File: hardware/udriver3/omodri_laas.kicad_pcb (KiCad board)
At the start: 6 copper layers, 50 x 50 mm, 219 parts, among them J1 Conn_01x11, J10 Conn_01x07, J11 Conn_01x03, J12 Conn_01x03, J13 Conn_01x02, J14 Conn_01x40, J2 Conn_01x05, J3 Conn_01x03, J4 Conn_01x03, J5 Conn_01x05, J6 Conn_01x05, J7 Conn_01x02, J8 Conn_01x07, J9 Conn_02x04_Odd_Even, Q1 CSD88599Q5DC, Q2 CSD88599Q5DC, Q3 CSD88599Q5DC, Q4 CSD88599Q5DC, Q5 CSD88599Q5DC, Q6 CSD88599Q5DC, Q7 NX7002BKM, SW1 B3U-3100P, U1 TMS320F28388D, U10 DSLVDS1048, U11 TPS3703, U12 TPS3703, U13 TPD6E05U06, U14 DSLVDS1047, U15 TPD2E001, U16 TPD3E001, U19 DRV8353S, U2 MAX17502FxTB, U20 DRV8353S, U3 MPM3804GG, U4 MPM3804GG, U5 LT6654AIS6-3, U6 TPD3E001, U7 TXB0106, U8 TCAN332G, U9 TPD6E05U06, X1 ECS-TXO-2016-33-200-TR

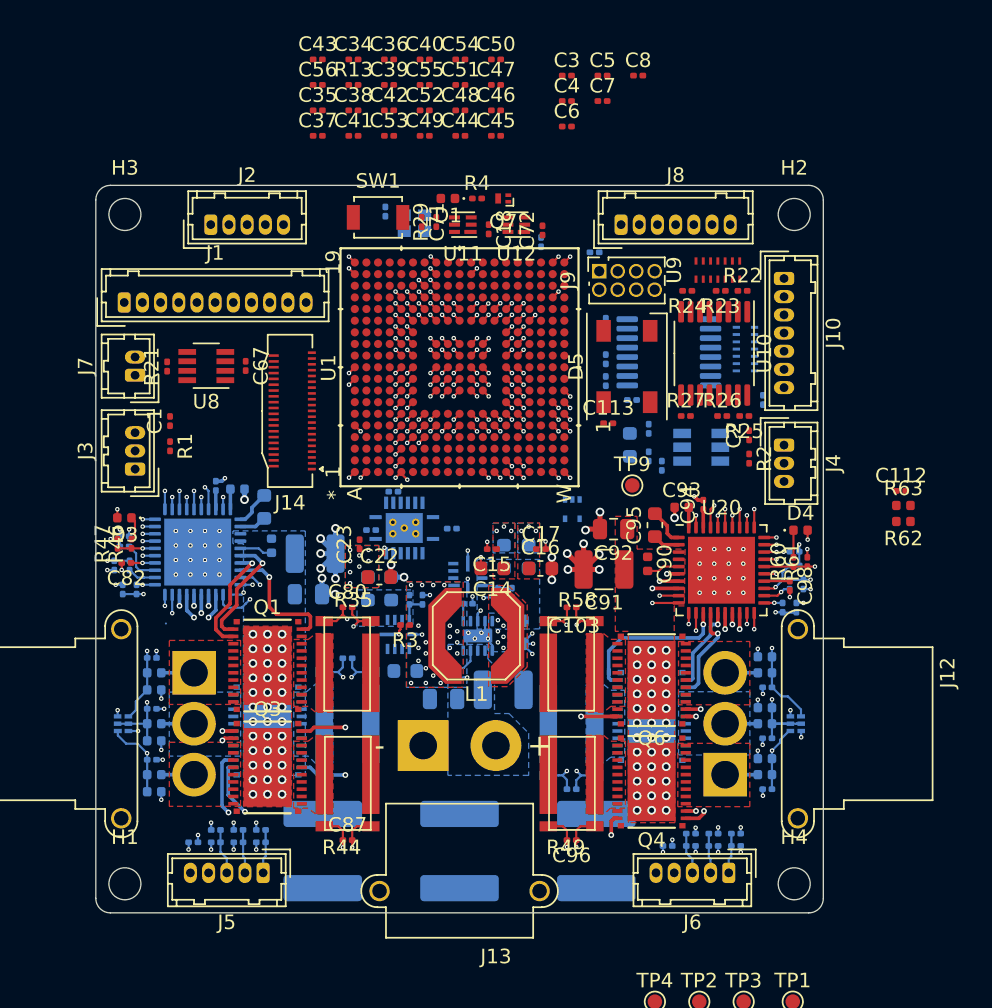
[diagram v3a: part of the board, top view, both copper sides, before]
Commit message: Routing update. All analog and DRV signals are wired. TMS mcu decoupling capacitors are in place.
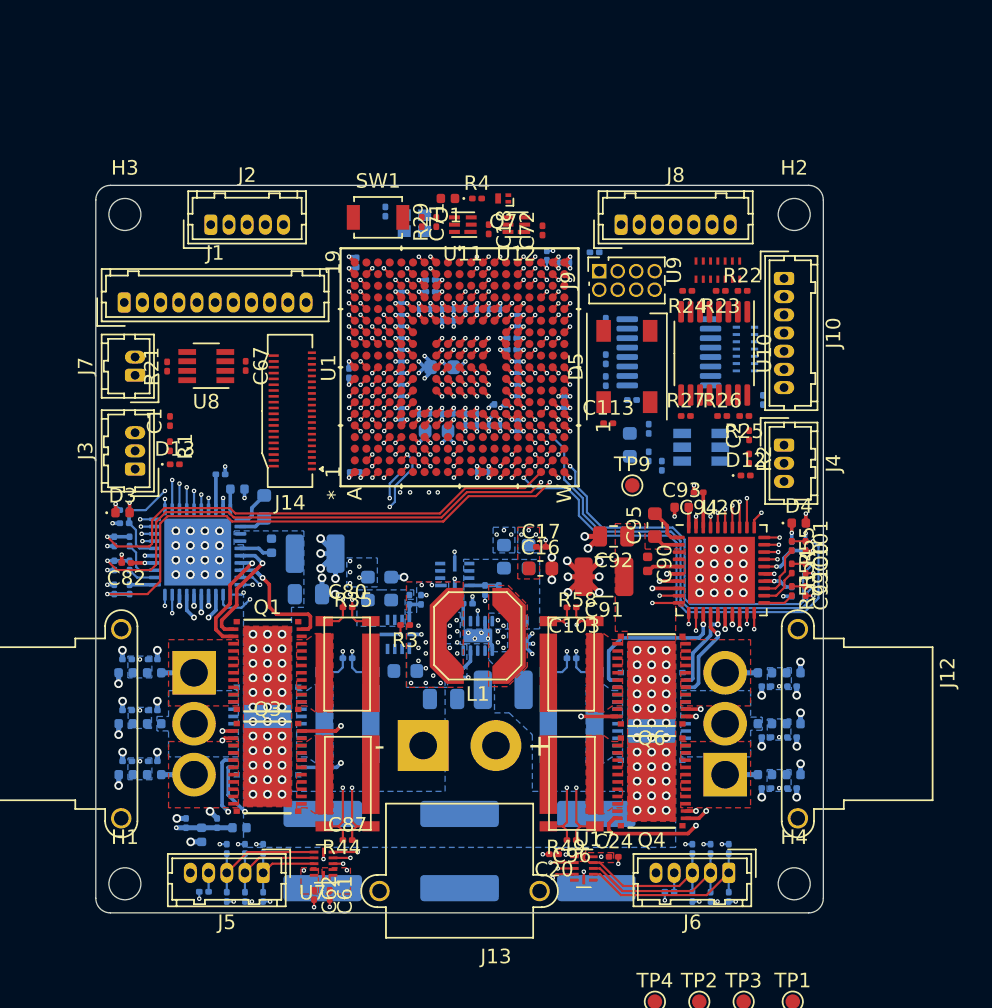
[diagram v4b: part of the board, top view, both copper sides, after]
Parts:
- removed R20: 1k, Resistor_SMD:R_0201_0603Metric
- removed U15: TPD2E001, Package_SO:Texas_R-PDSO-N5
- removed U16, U6: TPD3E001, udriver3:USON_6
- added C20: 100nF, Capacitor_SMD:C_0201_0603Metric, F.Cu at (131.5, 96.0)
- added C24: 100nF, Capacitor_SMD:C_0201_0603Metric, F.Cu at (135.6, 96.1)
- added D10: TPD1E04U04, Diode_SMD:D_0201_0603Metric, B.Cu at (102.2, 86.1)
- added D11: TPD1E04U04, Diode_SMD:D_0201_0603Metric, B.Cu at (106.2, 93.8)
- added D12: TPD1E04U04, Diode_SMD:D_0201_0603Metric, F.Cu at (144.7, 69.9)
- added D13: TPD1E04U04, Diode_SMD:D_0201_0603Metric, F.Cu at (105.4, 69.2)
- added D2: TPD1E04U04, Diode_SMD:D_0201_0603Metric, B.Cu at (147.8, 84.4)
- added D6: TPD1E04U04, Diode_SMD:D_0201_0603Metric, B.Cu at (147.8, 91.4)
- added D7: TPD1E04U04, Diode_SMD:D_0201_0603Metric, B.Cu at (147.8, 87.9)
- added D8: TPD1E04U04, Diode_SMD:D_0201_0603Metric, B.Cu at (102.2, 89.6)
- added D9: TPD1E04U04, Diode_SMD:D_0201_0603Metric, B.Cu at (102.2, 82.6)
- added U17: LSF0204RUT, Package_DFN_QFN:Texas_R_PUQFN-N12, F.Cu at (133.5, 96.9)
- C100, C101, C61, C62, C99, R51, R54, R55: moved to F.Cu
- C112, C14, C15, C22, C23, C3, C34, C35, C36, C37, C38, C39, C4, C40, C41, C42, C43, C44, C45, C46, C47, C48, C49, C5, C50, C51, C52, C53, C54, C55, C56, C6, C7, C8, C98, R13, R46, R47, R60, R61, R62, R63: moved to B.Cu
- U7: value TXB0106 -> LSF0204RUT; footprint udriver3:PVQFN_17 -> Package_DFN_QFN:Texas_R_PUQFN-N12; moved to F.Cu
- moved R63 53.3 mm to (107.3, 94.6), turned to 270 degrees
- moved C112 52.3 mm to (108.3, 93.8), turned to 90 degrees
- moved R62 50.3 mm to (109.9, 94.2)
- moved C54 28.4 mm to (126.6, 69.7)
- moved C61 28.1 mm to (116.1, 98.8), turned to 270 degrees
- moved C36 25.8 mm to (125.8, 66.5)
- moved C62 25.4 mm to (115.0, 98.8), turned to 270 degrees
- moved C43 25.0 mm to (121.0, 65.7), turned to 270 degrees
- moved R13 24.0 mm to (125.8, 65.7)
- moved C55 23.8 mm to (132.2, 64.9), turned to 270 degrees
- moved C50 23.8 mm to (117.4, 62.9), turned to 90 degrees
- moved U7 23.7 mm to (115.7, 96.6), turned to 180 degrees
- moved C3 23.3 mm to (128.2, 65.4), turned to 90 degrees
- moved C53 23.2 mm to (117.8, 69.7), turned to 180 degrees
- moved C4 22.6 mm to (129.0, 66.5), turned to 270 degrees
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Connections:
- R56 pad 1: GND -> Net-(Q5-Pad12)
- R56 pad 2: /OMODRI_driver_M2/SNB -> /OMODRI_driver_M2/SPB
- R56 pad 3: /OMODRI_driver_M2/SPB -> /OMODRI_driver_M2/SNB
- R56 pad 4: Net-(Q5-Pad12) -> GND
- U7 pad 1: /OMODRI_GPIO/ENC1_CHA -> VDD_3V3
- U7 pad 10: /OMODRI_QuadEncod/ENC2_A -> Net-(U7-Pad10)
- U7 pad 11: /OMODRI_QuadEncod/ENC2_B -> 5V0
- U7 pad 12: /OMODRI_QuadEncod/ENC2_I -> VDD_3V3
- U7 pad 2: VDD_3V3 -> Net-(U7-Pad2)
- U7 pad 3: /OMODRI_GPIO/ENC1_CHB -> /OMODRI_GPIO/ENC1_CHA
- U7 pad 4: /OMODRI_GPIO/ENC1_CHI -> /OMODRI_GPIO/ENC1_CHB
- U7 pad 5: /OMODRI_GPIO/ENC2_CHI -> /OMODRI_GPIO/ENC1_CHI
- U7 pad 6: /OMODRI_GPIO/ENC2_CHB -> GND
- U7 pad 7: /OMODRI_GPIO/ENC2_CHA -> /OMODRI_QuadEncod/ENC1_I
- U7 pad 8: Net-(R20-Pad2) -> /OMODRI_QuadEncod/ENC1_B
- U7 pad 9: GND -> /OMODRI_QuadEncod/ENC1_A
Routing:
- net /OMODRI_GPIO/M1_Vbus: track 0.00 -> 55.0 mm, vias 0 -> 2
- net /OMODRI_GPIO/M1_Vc: track 5.48 -> 49.5 mm, vias 1 -> 2
- net GND: track 97.4 -> 139.3 mm, vias 181 -> 209
- net /OMODRI_GPIO/M1_Ic: track 1.43 -> 42.7 mm, vias 1 -> 3
- net /OMODRI_GPIO/M1_Vb: track 4.66 -> 45.4 mm, vias 1 -> 2
- net /OMODRI_GPIO/ENC2_CHA: track 0.00 -> 36.8 mm, vias 0 -> 2
- net /OMODRI_GPIO/ENC1_CHI: track 0.00 -> 36.4 mm, vias 0 -> 2
- net /OMODRI_GPIO/M1_Ib: track 1.52 -> 37.9 mm, vias 1 -> 3
- net /OMODRI_GPIO/ENC1_CHB: track 0.00 -> 36.1 mm, vias 0 -> 2
- net /OMODRI_GPIO/M1_Va: track 5.07 -> 40.9 mm, vias 1 -> 3
- net /OMODRI_GPIO/ENC1_CHA: track 0.00 -> 35.1 mm, vias 0 -> 2
- net /OMODRI_GPIO/ENC2_CHB: track 0.00 -> 34.3 mm, vias 0 -> 2
- net /OMODRI_GPIO/M1_Ia: track 1.18 -> 35.0 mm
- net /OMODRI_GPIO/ENC2_CHI: track 0.00 -> 33.4 mm, vias 0 -> 2
- net /OMODRI_driver_M2/INHA: track 0.84 -> 33.2 mm, vias 1 -> 3
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- added copper zone on B.Cu, net /OMODRI_GPIO/M1_Va
- added copper zone on B.Cu, net /OMODRI_GPIO/M1_Vb
- added copper zone on B.Cu, net /OMODRI_GPIO/M1_Vc
- added copper zone on B.Cu, net /OMODRI_GPIO/M2_Va
- added copper zone on B.Cu, net /OMODRI_GPIO/M2_Vb
- added copper zone on B.Cu, net /OMODRI_GPIO/M2_Vc
- added copper zone on GND.Cu, net GND
- removed copper zone on F.Cu, net VDD_1V2
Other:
- copper layers 6 -> 8

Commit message: First release of the fully routed OMODRI PCB from LAAS. (8 layers)
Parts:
- removed C113: 100nF, Capacitor_SMD:C_0201_0603Metric
- removed J14: Conn_01x40, Connector_FFC-FPC:JAE_FF0841SA1_2Rows-41Pins_P0.40mm_Horizontal
- removed TP1, TP2, TP3, TP4, TP9: TestPoint, TestPoint:TestPoint_Pad_D1.0mm
- added J15: ADM6_ADF6, udriver3:ADF6-10-XX.X-XXX-4-X-A-XR, B.Cu at (113.0, 65.0)
- added J16: ADM6_ADF6, udriver3:ADF6-10-XX.X-XXX-4-X-A-XR, B.Cu at (137.0, 65.0)
- added R7: 33, Resistor_SMD:R_0201_0603Metric, F.Cu at (126.8, 53.6)
- C1, C16, C17, C18, C72, D12, R1, R25, R26, R27, U11, U12: moved to B.Cu
- C69, R30: moved to F.Cu
- J1: footprint Connector_Hirose:Hirose_DF13-11P-1.25DSA_1x11_P1.25mm_Vertical -> udriver3:Hirose_DF13-11P-1.25DSA_1x11_P1.25mm_Vertical
- J10, J8: footprint Connector_Hirose:Hirose_DF13-07P-1.25DSA_1x07_P1.25mm_Vertical -> udriver3:Hirose_DF13-07P-1.25DSA_1x07_P1.25mm_Vertical
- J2, J5, J6: footprint Connector_Hirose:Hirose_DF13-05P-1.25DSA_1x05_P1.25mm_Vertical -> udriver3:Hirose_DF13-05P-1.25DSA_1x05_P1.25mm_Vertical
- J3, J4: footprint Connector_Hirose:Hirose_DF13-03P-1.25DSA_1x03_P1.25mm_Vertical -> udriver3:Hirose_DF13-03P-1.25DSA_1x03_P1.25mm_Vertical
- J7: footprint Connector_Hirose:Hirose_DF13-02P-1.25DSA_1x02_P1.25mm_Vertical -> udriver3:Hirose_DF13-02P-1.25DSA_1x02_P1.25mm_Vertical
- U2: footprint Package_DFN_QFN:TDFN-10-1EP_2x3mm_P0.5mm_EP0.9x2mm -> udriver3:TDFN-10-1EP_2x3mm_P0.5mm_EP0.9x2mm_ThermalVias
- X1: value ECS-TXO-2016-33-200-TR -> ECS-TXO-2016-33-250-TR; footprint Crystal:Crystal_SMD_2016-4Pin_2.0x1.6mm -> udriver3:Crystal_SMD_2016-4Pin_2.0x1.6mm; moved to F.Cu
- moved D12 38.8 mm to (105.9, 68.2), turned to 90 degrees
- moved D13 38.0 mm to (143.4, 69.5), turned to 90 degrees
- moved D5 28.7 mm to (108.2, 67.1), turned to 270 degrees
- moved C16 11.9 mm to (131.0, 64.4), turned to 90 degrees
- moved C18 10.3 mm to (119.0, 59.5), turned to 180 degrees
- moved C17 9.98 mm to (129.8, 64.9), turned to 90 degrees
- moved C73 9.04 mm to (133.8, 56.2), turned to 90 degrees
- moved U11 7.84 mm to (119.2, 57.6), turned to 90 degrees
- moved R30 7.65 mm to (127.2, 51.7), turned to 270 degrees
- moved C72 7.29 mm to (125.4, 58.1), turned to 270 degrees
- moved J9 7.24 mm to (128.9, 51.4)
- moved Q7 6.96 mm to (121.0, 51.2), turned to 90 degrees
- moved R31 5.99 mm to (132.2, 58.2), turned to 270 degrees
- moved C29 5.80 mm to (132.2, 66.5)
- moved C69 5.41 mm to (125.2, 52.9)
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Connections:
- net /JTAG + CLOCK + RESET/F2838x_CLK_20MHz renamed /JTAG + CLOCK + RESET/F2838x_CLK_25MHz
- net Net-(C74-Pad2) renamed /OMODRI_driver_M1/VCP_DRV
- net Net-(C79-Pad1) renamed /OMODRI_driver_M1/CPH
- net Net-(C79-Pad2) renamed /OMODRI_driver_M1/CPL
- net Net-(C90-Pad2) renamed /OMODRI_driver_M2/VCP_DRV
- net Net-(C95-Pad1) renamed /OMODRI_driver_M2/CPH
- net Net-(C95-Pad2) renamed /OMODRI_driver_M2/CPL
- net Net-(Q1-Pad12) renamed /OMODRI_driver_M1/OUT_M1_CH1
- net Net-(Q2-Pad12) renamed /OMODRI_driver_M1/OUT_M1_CH2
- net Net-(Q3-Pad12) renamed /OMODRI_driver_M1/OUT_M1_CH3
- net Net-(Q4-Pad12) renamed /OMODRI_driver_M2/OUT_M2_CH1
- net Net-(Q5-Pad12) renamed /OMODRI_driver_M2/OUT_M2_CH2
- net Net-(Q6-Pad12) renamed /OMODRI_driver_M2/OUT_M2_CH3
- net Net-(R28-Pad1) renamed /JTAG + CLOCK + RESET/ERRORSTS
- C1 pad 1: /OMODRI_GPIO/ANALOG_IN2 -> /OMODRI_GPIO/ANALOG_IN1
- C2 pad 1: /OMODRI_GPIO/ANALOG_IN1 -> /OMODRI_GPIO/ANALOG_IN2
- J1 pad 3: /OMODRI_GPIO/~COM_SPI_CSn~ -> /OMODRI_GPIO/~SPI_CSn~
- J1 pad 4: /OMODRI_GPIO/COM_SPI_SOMI -> /OMODRI_GPIO/SPI_SOMI
- J1 pad 5: /OMODRI_GPIO/COM_SPI_CLK -> /OMODRI_GPIO/SPI_CLK
- J1 pad 6: /OMODRI_GPIO/COM_SPI_SIMO -> /OMODRI_GPIO/SPI_SIMO
- J2 pad 2: /OMODRI_GPIO/~SPI_CSn~ -> /OMODRI_GPIO/~COM_SPI_CSn~
- J2 pad 3: /OMODRI_GPIO/SPI_SOMI -> /OMODRI_GPIO/COM_SPI_SOMI
- J2 pad 4: /OMODRI_GPIO/SPI_CLK -> /OMODRI_GPIO/COM_SPI_CLK
- J2 pad 5: /OMODRI_GPIO/SPI_SIMO -> /OMODRI_GPIO/COM_SPI_SIMO
- R1 pad 1: /OMODRI_GPIO/ANALOG_IN2 -> /OMODRI_GPIO/ANALOG_IN1
- R2 pad 1: /OMODRI_GPIO/ANALOG_IN1 -> /OMODRI_GPIO/ANALOG_IN2
- U1 pad A13: /OMODRI_GPIO/ESC_PHY1_LINKSTATUS -> /OMODRI_GPIO/GPIO3
- U1 pad A14: /OMODRI_GPIO/GPIO4 -> /OMODRI_GPIO/GPIO2
- U1 pad A15: /OMODRI_GPIO/GPIO2 -> /OMODRI_GPIO/GPIO1
- U1 pad B14: /OMODRI_GPIO/GPIO3 -> Net-(U1-PadB14)
- U1 pad B15: /OMODRI_GPIO/GPIO1 -> /OMODRI_GPIO/GPIO4
- U1 pad B5: Net-(U1-PadB5) -> /OMODRI_GPIO/WS2812B_CMD
- U1 pad C18: Net-(U1-PadC18) -> /OMODRI_GPIO/ESC_PHY1_LINKSTATUS
- U1 pad R16: Net-(U1-PadR16) -> /OMODRI_GPIO/ESC_PHY_CLK
- U1 pad T11: /OMODRI_GPIO/WS2812B_CMD -> Net-(U1-PadT11)
- U13 pad 1: /OMODRI_FSI_TX/TX_D1_LVDS_N -> /OMODRI_FSI_TX/TX_CLK_LVDS_N
- U13 pad 11: /OMODRI_FSI_TX/TX_D0_LVDS_N -> /OMODRI_FSI_TX/TX_D0_LVDS_P
- U13 pad 12: /OMODRI_FSI_TX/TX_D0_LVDS_P -> /OMODRI_FSI_TX/TX_D0_LVDS_N
- U13 pad 13: /OMODRI_FSI_TX/TX_D1_LVDS_P -> /OMODRI_FSI_TX/TX_CLK_LVDS_P
- U13 pad 14: /OMODRI_FSI_TX/TX_D1_LVDS_N -> /OMODRI_FSI_TX/TX_CLK_LVDS_N
- U13 pad 2: /OMODRI_FSI_TX/TX_D1_LVDS_P -> /OMODRI_FSI_TX/TX_CLK_LVDS_P
- U13 pad 3: /OMODRI_FSI_TX/TX_D0_LVDS_P -> /OMODRI_FSI_TX/TX_D0_LVDS_N
- U13 pad 4: /OMODRI_FSI_TX/TX_D0_LVDS_N -> /OMODRI_FSI_TX/TX_D0_LVDS_P
- U13 pad 6: /OMODRI_FSI_TX/TX_CLK_LVDS_P -> /OMODRI_FSI_TX/TX_D1_LVDS_P
- U13 pad 7: /OMODRI_FSI_TX/TX_CLK_LVDS_N -> /OMODRI_FSI_TX/TX_D1_LVDS_N
- U13 pad 8: /OMODRI_FSI_TX/TX_CLK_LVDS_N -> /OMODRI_FSI_TX/TX_D1_LVDS_N
- U13 pad 9: /OMODRI_FSI_TX/TX_CLK_LVDS_P -> /OMODRI_FSI_TX/TX_D1_LVDS_P
- U9 pad 1: /OMODRI_FSI_RX/RX_CLK_LVDS_N -> /OMODRI_FSI_RX/RX_D1_LVDS_N
- U9 pad 11: /OMODRI_FSI_RX/RX_D0_LVDS_P -> /OMODRI_FSI_RX/RX_D0_LVDS_N
- U9 pad 12: /OMODRI_FSI_RX/RX_D0_LVDS_N -> /OMODRI_FSI_RX/RX_D0_LVDS_P
- U9 pad 13: /OMODRI_FSI_RX/RX_CLK_LVDS_P -> /OMODRI_FSI_RX/RX_D1_LVDS_P
- U9 pad 14: /OMODRI_FSI_RX/RX_CLK_LVDS_N -> /OMODRI_FSI_RX/RX_D1_LVDS_N
- U9 pad 2: /OMODRI_FSI_RX/RX_CLK_LVDS_P -> /OMODRI_FSI_RX/RX_D1_LVDS_P
- U9 pad 3: /OMODRI_FSI_RX/RX_D0_LVDS_N -> /OMODRI_FSI_RX/RX_D0_LVDS_P
- U9 pad 4: /OMODRI_FSI_RX/RX_D0_LVDS_P -> /OMODRI_FSI_RX/RX_D0_LVDS_N
- U9 pad 6: /OMODRI_FSI_RX/RX_D1_LVDS_P -> /OMODRI_FSI_RX/RX_CLK_LVDS_P
- U9 pad 7: /OMODRI_FSI_RX/RX_D1_LVDS_N -> /OMODRI_FSI_RX/RX_CLK_LVDS_N
- U9 pad 8: /OMODRI_FSI_RX/RX_D1_LVDS_N -> /OMODRI_FSI_RX/RX_CLK_LVDS_N
- U9 pad 9: /OMODRI_FSI_RX/RX_D1_LVDS_P -> /OMODRI_FSI_RX/RX_CLK_LVDS_P
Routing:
- net GND: track 139.3 -> 203.4 mm, vias 209 -> 345
- net REF_3V0_BUF: track 5.96 -> 53.8 mm, vias 6 -> 8
- net /OMODRI_GPIO/~COM_SPI_CSn~: track 0.57 -> 45.1 mm, vias 1 -> 2
- net /OMODRI_GPIO/COM_SPI_SOMI: track 0.57 -> 43.6 mm, vias 1 -> 2
- net /OMODRI_GPIO/COM_SPI_CLK: track 0.57 -> 42.3 mm, vias 1 -> 2
- net VDDA_3V3: track 3.13 -> 40.2 mm, vias 5 -> 18
- net /OMODRI_GPIO/COM_SPI_SIMO: track 0.57 -> 37.4 mm, vias 1 -> 2
- net /OMODRI_GPIO/ANALOG_IN1: track 0.57 -> 34.7 mm, vias 1 -> 3
- net /OMODRI_GPIO/ESC_RX1_D3: track 0.55 -> 23.8 mm, vias 1 -> 2
- net /OMODRI_GPIO/ANALOG_IN2: track 0.57 -> 23.5 mm, vias 1 -> 3
- net /OMODRI_GPIO/ESC_RX1_D2: track 0.57 -> 22.7 mm, vias 1 -> 2
- net VDD_3V3: track 40.0 -> 61.6 mm, vias 44 -> 65
- net /OMODRI_GPIO/ESC_PHY1_LINKSTATUS: track 0.57 -> 22.1 mm, vias 1 -> 2
- net /OMODRI_GPIO/ESC_PHY_CLK_OSC: track 0.00 -> 20.8 mm, vias 0 -> 2
- net /OMODRI_GPIO/ESC_RX1_D1: track 0.57 -> 20.4 mm, vias 1 -> 2
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- added copper zone on In2.Cu, net 5V0
- added copper zone on B.Cu, net GND
- added copper zone on F.Cu, net GND
- added copper zone on In2.Cu, net GND
- added copper zone on In5.Cu, net GND
- added copper zone on B.Cu, net REF_3V0_BUF
- added copper zone on In2.Cu, net REF_3V0_BUF
- added copper zone on In5.Cu, net REF_3V0_BUF
- added copper zone on PWR.Cu, net VDDA_3V3
- added copper zone on PWR.Cu, net VDD_3V3
- removed copper zone on F.Cu, net VDDA_3V3
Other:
- net class Analog_sig added: clearance 0.1016, trace_width 0.15, via_dia 0.4, via_drill 0.2
- net class Default: clearance 0.127 -> 0.1016; trace_width 0.15 -> 0.1016; via_dia 0.31 -> 0.4; via_drill 0.15 -> 0.2
- net class Gnd_Vdd added: clearance 0.1016, trace_width 0.25, via_dia 0.4, via_drill 0.2
- net class Power removed
- net class Power_sig added: clearance 0.15, trace_width 0.25, via_dia 0.4, via_drill 0.2
- rule trace_clearance: 0.127 -> 0.1016
- rule trace_min: 0.127 -> 0.1016
- rule via_min_size: 0.3032 -> 0.3048

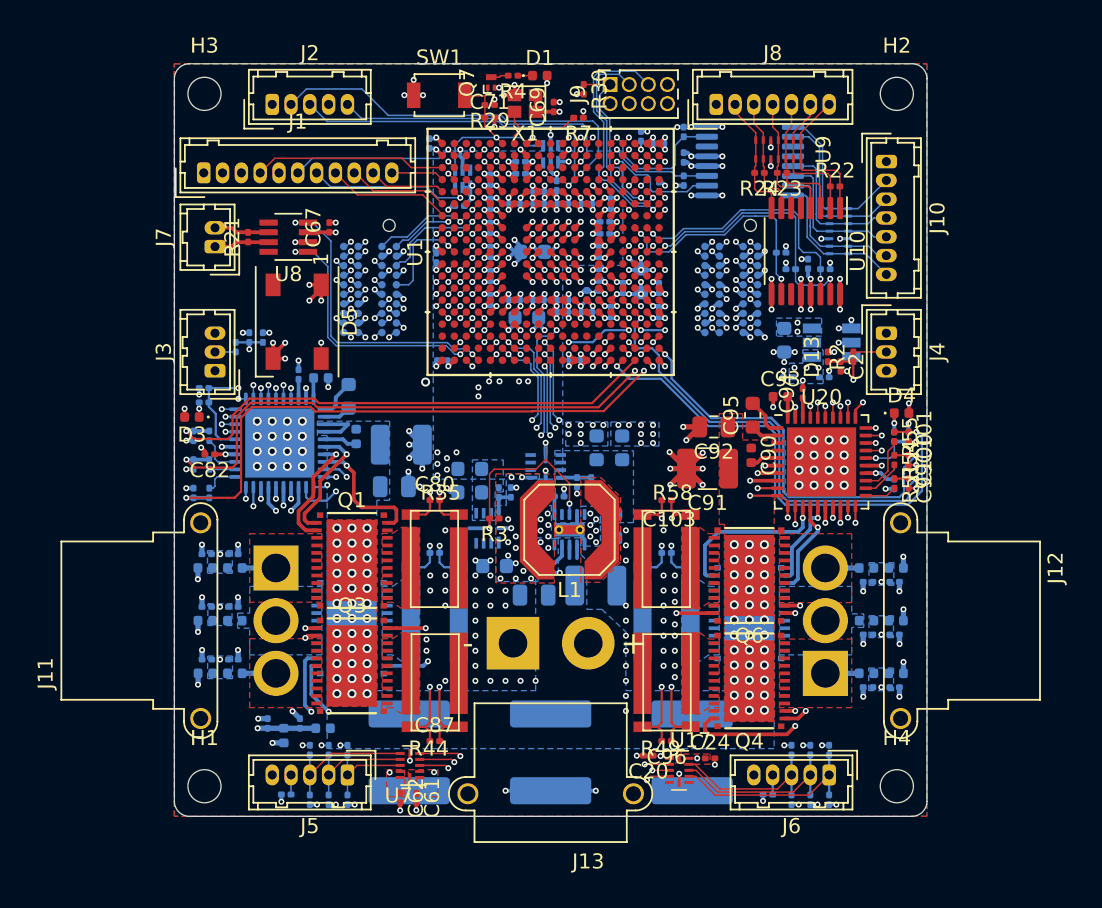
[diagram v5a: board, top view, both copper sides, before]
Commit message: Release of the fully routed OMODRI PCB from LAAS in 6 layers design.
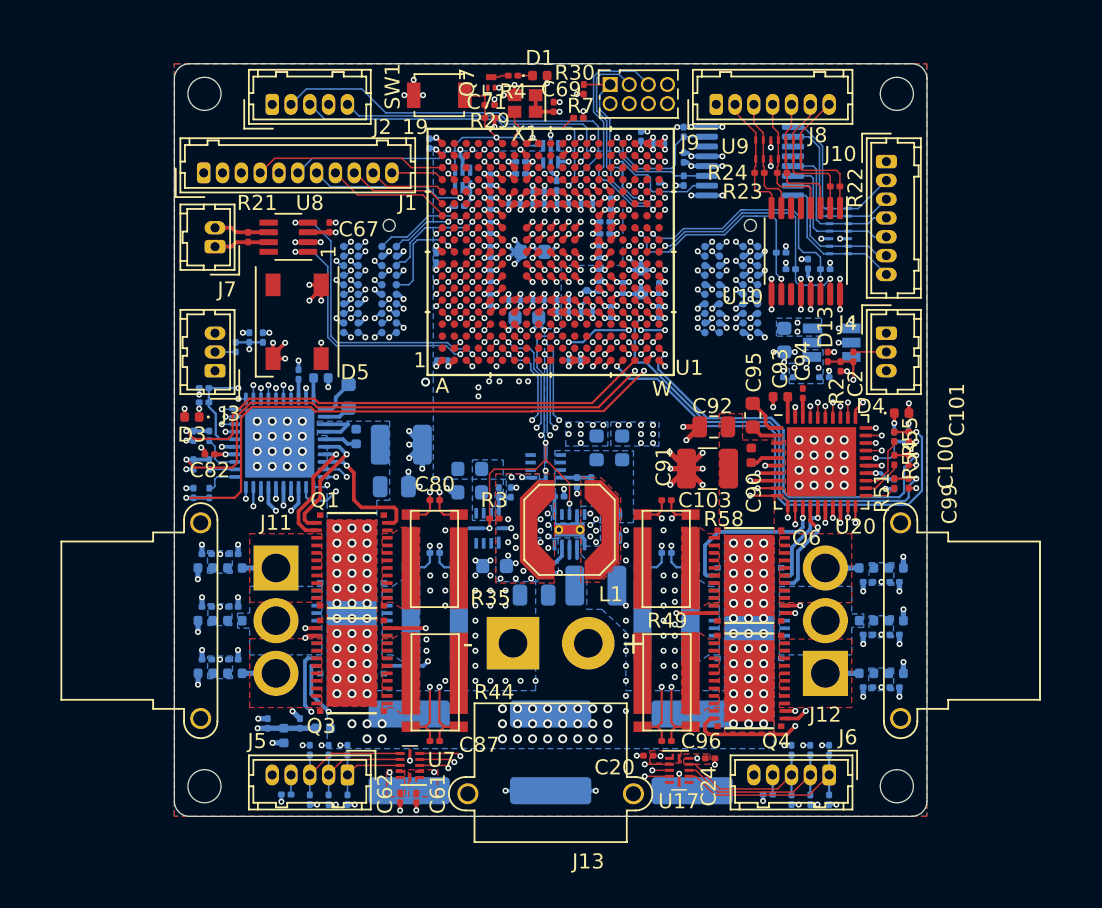
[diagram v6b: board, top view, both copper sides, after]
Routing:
- net /OMODRI_GPIO/COM_SPI_SOMI: track 43.6 -> 44.3 mm
- net /OMODRI_GPIO/~COM_SPI_CSn~: track 45.1 -> 45.7 mm
- net /OMODRI_GPIO/M2_Ib: track 33.9 -> 34.4 mm
- net GND: track 203.4 -> 203.7 mm, vias 345 -> 355
- net VPOWER: vias 72 -> 104
- net VDD_1V2: vias 27 -> 21
- added copper zone on In3.Cu, net GND
- added copper zone on In3.Cu, net REF_3V0_BUF
- added copper zone on In2.Cu, net VPOWER
- added copper zone on In3.Cu, net VPOWER
- added copper zone on PWR.Cu, net VPOWER
- removed copper zone on In5.Cu, net GND
- removed copper zone on In5.Cu, net REF_3V0_BUF
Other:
- copper layers 8 -> 6
